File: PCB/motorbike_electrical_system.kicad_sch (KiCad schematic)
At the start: 12 parts, among them U1 L7805, U2 L7805, U3 L7805, U4 ATmega16L-8P

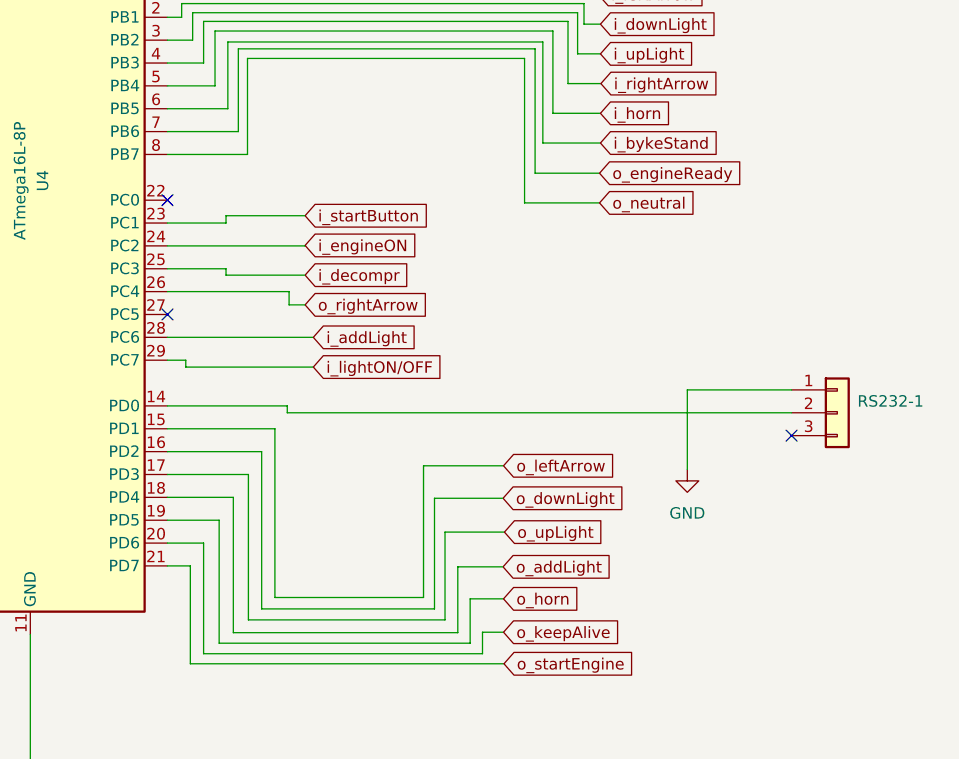
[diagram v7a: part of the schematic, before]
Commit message: RS232 TxD line added
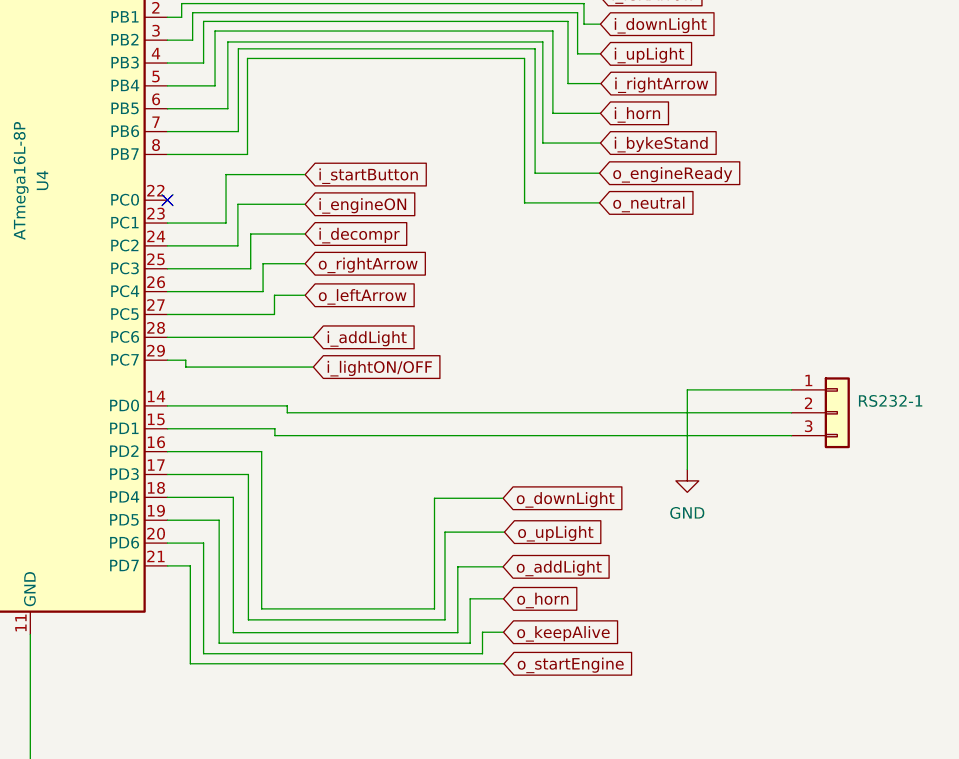
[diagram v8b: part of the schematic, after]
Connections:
- net o_leftArrow: now also U4.27 (PC5); no longer U4.15 (PD1)
- net at RS232-1.3 (Pin_3): now also U4.15 (PD1)
- no-connect marks 8 -> 6
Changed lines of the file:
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@@
   (no_connect (at 142.6464 99.822))
   (no_connect (at 142.6464 66.802))
-  (no_connect (at 211.9884 125.984))
-  (no_connect (at 142.6464 112.522))
   (no_connect (at 129.9464 46.482))
   (no_connect (at 142.6464 64.262))
@@
     (stroke (width 0) (type default) (color 0 0 0 0))
   )
+  (wire (pts (xy 154.5336 112.522) (xy 142.6464 112.522))
+    (stroke (width 0) (type default) (color 0 0 0 0))
+  )
   (wire (pts (xy 127.4064 39.37) (xy 127.4064 46.482))
     (stroke (width 0) (type default) (color 0 0 0 0))
@@
     (stroke (width 0) (type default) (color 0 0 0 0))
   )
-  (wire (pts (xy 149.1488 107.442) (xy 149.1488 108.1532))
-    (stroke (width 0) (type default) (color 0 0 0 0))
-  )
   (wire (pts (xy 150.5204 83.0072) (xy 150.5204 92.202))
     (stroke (width 0) (type default) (color 0 0 0 0))
@@
     (stroke (width 0) (type default) (color 0 0 0 0))
   )
-  (wire (pts (xy 154.5844 125.222) (xy 154.5844 143.9672))
+  (wire (pts (xy 154.5844 125.222) (xy 154.5844 125.984))
     (stroke (width 0) (type default) (color 0 0 0 0))
   )
@@
     (stroke (width 0) (type default) (color 0 0 0 0))
   )
-  (wire (pts (xy 149.1488 102.362) (xy 149.1488 101.5492))
+  (wire (pts (xy 149.1488 102.362) (xy 149.1488 96.9772))
     (stroke (width 0) (type default) (color 0 0 0 0))
   )
@@
     (stroke (width 0) (type default) (color 0 0 0 0))
   )
-  (wire (pts (xy 142.6464 109.982) (xy 156.1592 109.982))
+  (wire (pts (xy 142.6464 109.982) (xy 153.2636 109.982))
     (stroke (width 0) (type default) (color 0 0 0 0))
   )
@@
     (stroke (width 0) (type default) (color 0 0 0 0))
   )
+  (wire (pts (xy 157.9372 106.8832) (xy 153.2636 106.8832))
+    (stroke (width 0) (type default) (color 0 0 0 0))
+  )
   (wire (pts (xy 142.6464 76.962) (xy 190.5 76.962))
     (stroke (width 0) (type default) (color 0 0 0 0))
   )
-  (wire (pts (xy 156.1592 109.982) (xy 156.1592 111.4552))
-    (stroke (width 0) (type default) (color 0 0 0 0))
-  )
-  (wire (pts (xy 157.9372 104.902) (xy 157.9372 104.8512))
-    (stroke (width 0) (type default) (color 0 0 0 0))
-  )
   (wire (pts (xy 188.9252 77.978) (xy 188.9252 80.264))
     (stroke (width 0) (type default) (color 0 0 0 0))
   )
+  (wire (pts (xy 150.4696 100.2792) (xy 150.4696 104.902))
+    (stroke (width 0) (type default) (color 0 0 0 0))
+  )
   (wire (pts (xy 142.6464 61.722) (xy 186.182 61.722))
     (stroke (width 0) (type default) (color 0 0 0 0))
@@
     (stroke (width 0) (type default) (color 0 0 0 0))
   )
-  (wire (pts (xy 142.6464 104.902) (xy 157.9372 104.902))
+  (wire (pts (xy 142.6464 104.902) (xy 150.4696 104.902))
     (stroke (width 0) (type default) (color 0 0 0 0))
   )
@@
     (stroke (width 0) (type default) (color 0 0 0 0))
   )
+  (wire (pts (xy 151.892 103.5812) (xy 151.892 107.442))
+    (stroke (width 0) (type default) (color 0 0 0 0))
+  )
   (wire (pts (xy 142.6464 125.222) (xy 154.5844 125.222))
     (stroke (width 0) (type default) (color 0 0 0 0))
@@
     (stroke (width 0) (type default) (color 0 0 0 0))
   )
+  (wire (pts (xy 157.9372 100.2792) (xy 150.4696 100.2792))
+    (stroke (width 0) (type default) (color 0 0 0 0))
+  )
   (wire (pts (xy 197.9168 47.7012) (xy 204.7748 47.7012))
     (stroke (width 0) (type default) (color 0 0 0 0))
   )
-  (wire (pts (xy 142.6464 107.442) (xy 149.1488 107.442))
+  (wire (pts (xy 142.6464 107.442) (xy 151.892 107.442))
     (stroke (width 0) (type default) (color 0 0 0 0))
   )
@@
     (stroke (width 0) (type default) (color 0 0 0 0))
   )
-  (wire (pts (xy 149.1488 108.1532) (xy 157.9372 108.1532))
-    (stroke (width 0) (type default) (color 0 0 0 0))
-  )
   (wire (pts (xy 142.6464 89.662) (xy 149.352 89.662))
     (stroke (width 0) (type default) (color 0 0 0 0))
@@
     (stroke (width 0) (type default) (color 0 0 0 0))
   )
-  (wire (pts (xy 156.1592 111.4552) (xy 157.9372 111.4552))
-    (stroke (width 0) (type default) (color 0 0 0 0))
-  )
   (wire (pts (xy 186.182 58.0644) (xy 194.1068 58.0644))
     (stroke (width 0) (type default) (color 0 0 0 0))
   )
+  (wire (pts (xy 154.5336 110.3884) (xy 157.9372 110.3884))
+    (stroke (width 0) (type default) (color 0 0 0 0))
+  )
   (wire (pts (xy 145.1864 151.3332) (xy 180.0352 151.3332))
     (stroke (width 0) (type default) (color 0 0 0 0))
@@
     (stroke (width 0) (type default) (color 0 0 0 0))
   )
-  (wire (pts (xy 179.9844 129.3368) (xy 171.0944 129.3368))
+  (wire (pts (xy 149.1488 96.9772) (xy 157.9372 96.9772))
     (stroke (width 0) (type default) (color 0 0 0 0))
   )
@@
     (stroke (width 0) (type default) (color 0 0 0 0))
   )
+  (wire (pts (xy 153.2636 106.8832) (xy 153.2636 109.982))
+    (stroke (width 0) (type default) (color 0 0 0 0))
+  )
   (wire (pts (xy 142.6464 69.342) (xy 148.6408 69.342))
     (stroke (width 0) (type default) (color 0 0 0 0))
@@
     (stroke (width 0) (type default) (color 0 0 0 0))
   )
-  (wire (pts (xy 171.0944 143.9672) (xy 154.5844 143.9672))
-    (stroke (width 0) (type default) (color 0 0 0 0))
-  )
   (wire (pts (xy 149.352 82.2452) (xy 184.3532 82.2452))
     (stroke (width 0) (type default) (color 0 0 0 0))
@@
     (stroke (width 0) (type default) (color 0 0 0 0))
   )
-  (wire (pts (xy 171.0944 129.3368) (xy 171.0944 143.9672))
-    (stroke (width 0) (type default) (color 0 0 0 0))
-  )
   (wire (pts (xy 181.7624 59.182) (xy 181.8132 52.9844))
     (stroke (width 0) (type default) (color 0 0 0 0))
@@
     (stroke (width 0) (type default) (color 0 0 0 0))
   )
+  (wire (pts (xy 157.9372 103.5812) (xy 151.892 103.5812))
+    (stroke (width 0) (type default) (color 0 0 0 0))
+  )
   (wire (pts (xy 30.988 185.42) (xy 37.211 185.42))
     (stroke (width 0) (type default) (color 0 0 0 0))
@@
     (stroke (width 0) (type default) (color 0 0 0 0))
   )
-  (wire (pts (xy 149.1488 101.5492) (xy 157.9372 101.5492))
-    (stroke (width 0) (type default) (color 0 0 0 0))
-  )
   (wire (pts (xy 72.771 184.15) (xy 72.771 185.42))
     (stroke (width 0) (type default) (color 0 0 0 0))
@@
     (stroke (width 0) (type default) (color 0 0 0 0))
   )
+  (wire (pts (xy 154.5336 110.3884) (xy 154.5336 112.522))
+    (stroke (width 0) (type default) (color 0 0 0 0))
+  )
   (wire (pts (xy 37.211 169.672) (xy 37.211 175.26))
     (stroke (width 0) (type default) (color 0 0 0 0))
@@
   )
   (wire (pts (xy 177.6476 147.828) (xy 179.9844 147.828))
+    (stroke (width 0) (type default) (color 0 0 0 0))
+  )
+  (wire (pts (xy 154.5844 125.984) (xy 211.9884 125.984))
     (stroke (width 0) (type default) (color 0 0 0 0))
   )
@@
     )
   )
-  (global_label "o_leftArrow" (shape input) (at 179.9844 129.3368 0) (fields_autoplaced)
-    (effects (font (size 1.27 1.27)) (justify left))
-    (property "Riferimenti inter-foglio" "${INTERSHEET_REFS}" (id 0) (at 192.8599 129.2574 0)
+  (global_label "o_leftArrow" (shape input) (at 157.9372 110.3884 0) (fields_autoplaced)
+    (effects (font (size 1.27 1.27)) (justify left))
+    (property "Riferimenti inter-foglio" "${INTERSHEET_REFS}" (id 0) (at 170.8127 110.309 0)
       (effects (font (size 1.27 1.27)) (justify left) hide)
     )
@@
     )
   )
-  (global_label "i_decompr" (shape input) (at 157.9372 108.1532 0) (fields_autoplaced)
-    (effects (font (size 1.27 1.27)) (justify left))
-    (property "Riferimenti inter-foglio" "${INTERSHEET_REFS}" (id 0) (at 170.0265 108.0738 0)
+  (global_label "i_decompr" (shape input) (at 157.9372 103.5812 0) (fields_autoplaced)
+    (effects (font (size 1.27 1.27)) (justify left))
+    (property "Riferimenti inter-foglio" "${INTERSHEET_REFS}" (id 0) (at 170.0265 103.5018 0)
       (effects (font (size 1.27 1.27)) (justify left) hide)
     )
@@
     )
   )
-  (global_label "o_rightArrow" (shape input) (at 157.9372 111.4552 0) (fields_autoplaced)
-    (effects (font (size 1.27 1.27)) (justify left))
-    (property "Riferimenti inter-foglio" "${INTERSHEET_REFS}" (id 0) (at 172.0222 111.3758 0)
+  (global_label "o_rightArrow" (shape input) (at 157.9372 106.8832 0) (fields_autoplaced)
+    (effects (font (size 1.27 1.27)) (justify left))
+    (property "Riferimenti inter-foglio" "${INTERSHEET_REFS}" (id 0) (at 172.0222 106.8038 0)
       (effects (font (size 1.27 1.27)) (justify left) hide)
     )
@@
     )
   )
-  (global_label "i_startButton" (shape input) (at 157.9372 101.5492 0) (fields_autoplaced)
-    (effects (font (size 1.27 1.27)) (justify left))
-    (property "Riferimenti inter-foglio" "${INTERSHEET_REFS}" (id 0) (at 172.506 101.4698 0)
+  (global_label "i_startButton" (shape input) (at 157.9372 96.9772 0) (fields_autoplaced)
+    (effects (font (size 1.27 1.27)) (justify left))
+    (property "Riferimenti inter-foglio" "${INTERSHEET_REFS}" (id 0) (at 172.506 96.8978 0)
       (effects (font (size 1.27 1.27)) (justify left) hide)
     )
@@
     )
   )
-  (global_label "i_engineON" (shape input) (at 157.9372 104.8512 0) (fields_autoplaced)
-    (effects (font (size 1.27 1.27)) (justify left))
-    (property "Riferimenti inter-foglio" "${INTERSHEET_REFS}" (id 0) (at 170.8127 104.7718 0)
-      (effects (font (size 1.27 1.27)) (justify left) hide)
-    )
+  (global_label "i_engineON" (shape input) (at 157.9372 100.2792 0) (fields_autoplaced)
+    (effects (font (size 1.27 1.27)) (justify left))
+    (property "Riferimenti inter-foglio" "${INTERSHEET_REFS}" (id 0) (at 170.8127 100.1998 0)
+      (effects (font (size 1.27 1.27)) (justify left) hide)
+    )
